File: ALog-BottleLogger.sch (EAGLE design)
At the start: 107 parts, among them IC2 ATMEGA644M, J6 5.5x2.1mm Barrel, Q10 MOSFET_PCH-IRLML2244, Q11 MOSFET-NCH-BSS138, Q12 MOSFET_PCH-IRLML2244, Q13 MOSFET-NCH-BSS138, Q5 MOSFET_PCH-IRLML2244, Q7 MOSFET_PCH-IRLML2244, Q8 MOSFET-NCH-BSS138, Q9 MOSFET-NCH-BSS138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

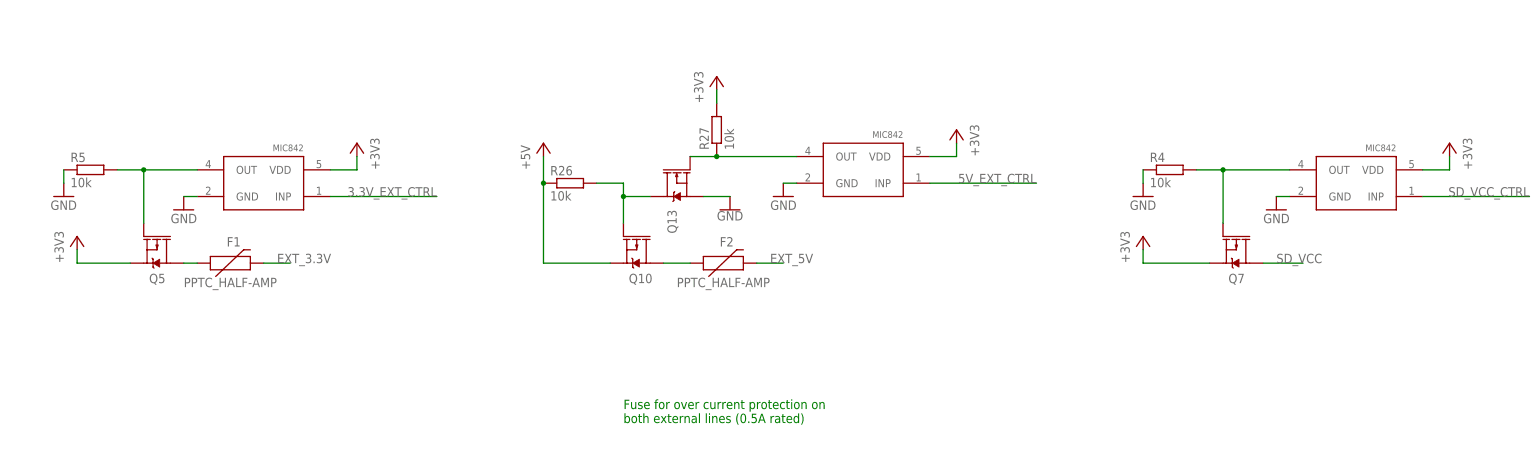
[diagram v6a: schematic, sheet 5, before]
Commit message: Add comparators for power control, change header layout adding more I2C, change clock power supply
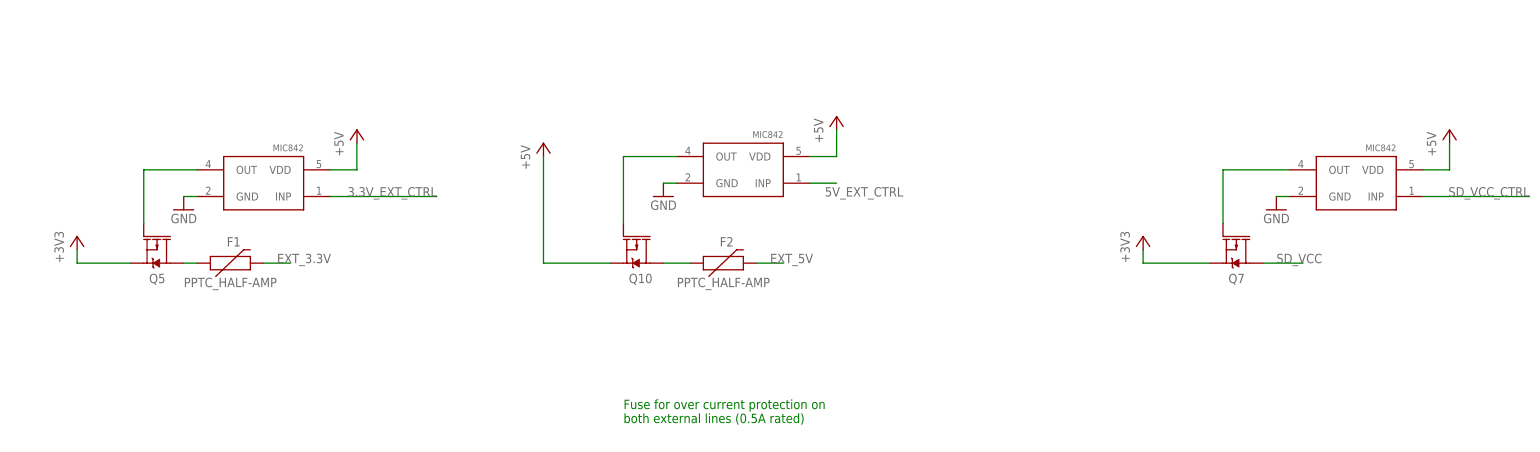
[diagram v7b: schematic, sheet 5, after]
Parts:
- removed Q13: MOSFET-NCH-BSS138, bschulz:MOSFET-NCH-BSS138
- removed R26: 10k, bschulz_passives:R-EU_10KR0603
- removed R27: 10k, bschulz:R-EU_10KR0603
- removed R4, R5: 10k, rcl:R-EU_R0603
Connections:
- removed net N$23: Q10.G, Q13.D, R26.2
- net +3V3: no longer R27.2, U$1.VDD, U$12.VDD, U$16.VDD
- net +5V: now also U$1.VDD, U$12.VDD, U$16.VDD; no longer R26.1
- net EXT_5V: no longer J16.3
- net GND: now also J16.3; no longer Q13.S, R4.1, R5.1
- net N$14: now also Q10.G; no longer Q13.G, R27.1
- net N$19: no longer R4.2
- net N$6: no longer R5.2

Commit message: update botton pad sizes
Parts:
- S1, U$4: value SKRPABE010 -> SWITCHC&K_400GF; device bschulz:SKRPABE010 -> bschulz_Old:SWITCHC&K_400GF
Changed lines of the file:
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@@
 <?xml version="1.0" encoding="utf-8"?>
 <!DOCTYPE eagle SYSTEM "eagle.dtd">
-<eagle version="8.4.3">
+<eagle version="8.4.1">
 <drawing>
 <settings>
@@
 <part name="C10" library="bschulz_passives" deviceset="C-EU" device="C0805" technology="22UF" value="22uF"/>
 <part name="R1" library="bschulz_passives" deviceset="R-EU_" device="R0603" technology="10K" value="10k"/>
-<part name="U$4" library="bschulz" deviceset="SKRPABE010" device=""/>
+<part name="U$4" library="bschulz_Old" deviceset="SWITCH" device="C&amp;K_400GF"/>
 <part name="GND12" library="supply1" deviceset="GND" device=""/>
 <part name="GND15" library="supply1" deviceset="GND" device=""/>
@@
 <part name="D1" library="semicon-smd-ipc" deviceset="DIODE_AC-CA_" device="" value="BAT54C"/>
 <part name="GND52" library="supply1" deviceset="GND" device=""/>
-<part name="S1" library="bschulz" deviceset="SKRPABE010" device=""/>
+<part name="S1" library="bschulz_Old" deviceset="SWITCH" device="C&amp;K_400GF"/>
 <part name="R18" library="bschulz_passives" deviceset="R-EU_" device="R0603" technology="1.62M" value="1.62M"/>
 <part name="R19" library="bschulz_passives" deviceset="R-EU_" device="R0603" technology="180K" value="180k"/>
